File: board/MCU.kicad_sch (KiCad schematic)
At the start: 23 parts, among them SW1 SW_Push, U1 STSPIN32G4TR

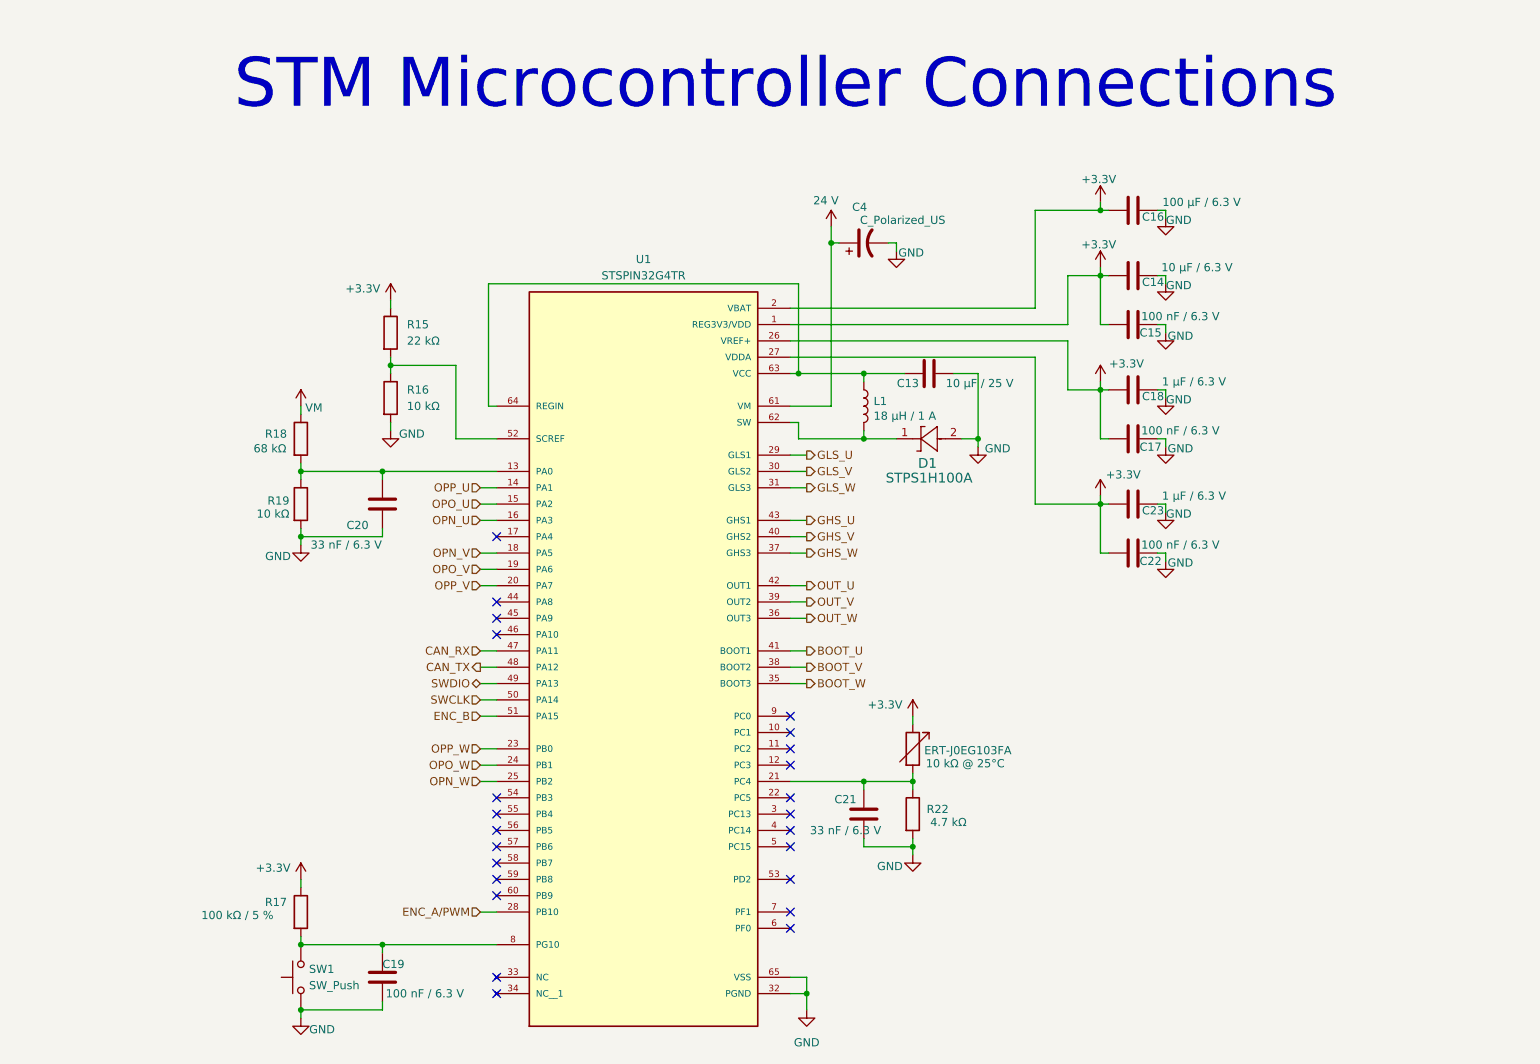
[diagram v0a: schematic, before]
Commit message: Fixed everything mentioned in schematic review, should be ready for second review/layout.
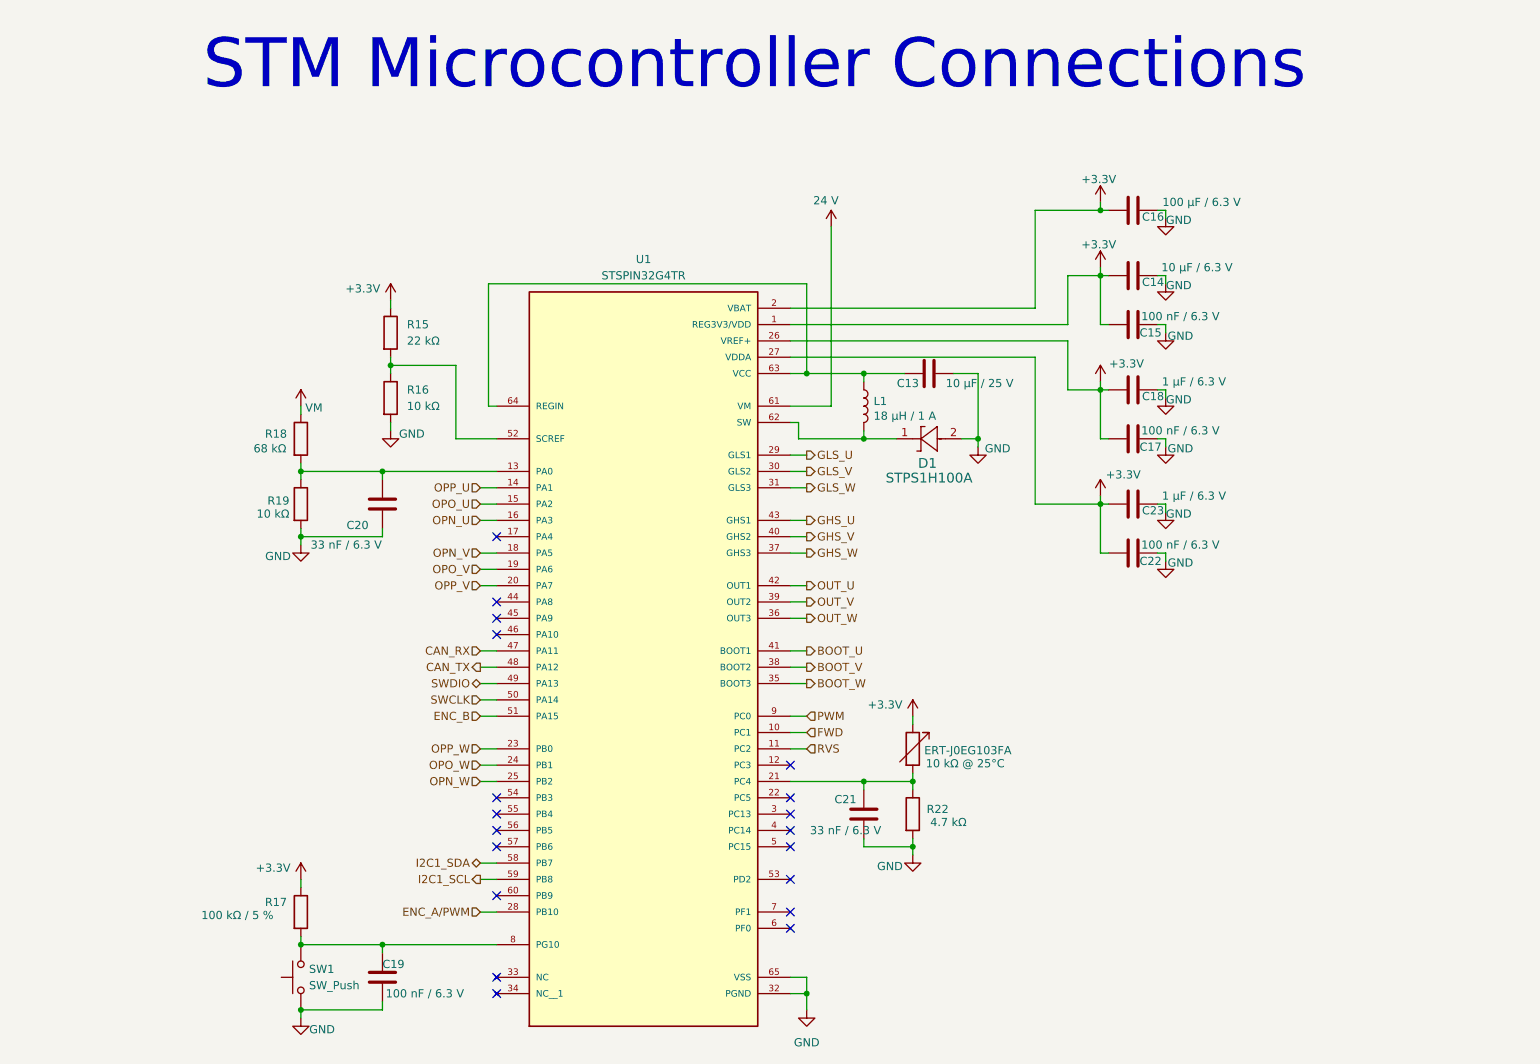
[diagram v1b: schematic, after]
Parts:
- removed C4: C_Polarized_US, symbol Device:C_Polarized_US
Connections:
- net FWD: now reaches U1.10 (PC1)
- net RVS: now reaches U1.11 (PC2)
- net I2C1_SDA: now reaches U1.58 (PB7)
- net I2C1_SCL: now reaches U1.59 (PB8)
- net PWM: now reaches U1.9 (PC0)
- no-connect marks 24 -> 19
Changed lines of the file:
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@@
 	(text "STM Microcontroller Connections\n"
 		(exclude_from_sim no)
-		(at 144.018 28.702 0)
+		(at 139.192 25.654 0)
 		(effects
 			(font
@@
 	)
 	(junction
-		(at 146.05 73.66)
+		(at 147.32 73.66)
 		(diameter 0)
 		(color 0 0 0 0)
@@
 	)
 	(junction
-		(at 151.13 53.34)
-		(diameter 0)
-		(color 0 0 0 0)
-	)
-	(junction
 		(at 156.21 83.82)
 		(diameter 0)
@@
 	)
 	(no_connect
-		(at 144.78 127)
-	)
-	(no_connect
 		(at 99.06 167.64)
 	)
@@
 	)
 	(no_connect
-		(at 144.78 132.08)
-	)
-	(no_connect
 		(at 144.78 147.32)
 	)
@@
 	)
 	(no_connect
-		(at 99.06 152.4)
-	)
-	(no_connect
-		(at 144.78 129.54)
-	)
-	(no_connect
 		(at 99.06 139.7)
 	)
@@
 	)
 	(no_connect
-		(at 99.06 149.86)
-	)
-	(no_connect
 		(at 144.78 157.48)
 	)
@@
 	(wire
 		(pts
-			(xy 151.13 53.34) (xy 152.4 53.34)
+			(xy 96.52 101.6) (xy 99.06 101.6)
 		)
 		(stroke
@@
 	(wire
 		(pts
-			(xy 96.52 101.6) (xy 99.06 101.6)
+			(xy 144.78 119.38) (xy 147.32 119.38)
 		)
 		(stroke
@@
 	(wire
 		(pts
-			(xy 144.78 119.38) (xy 147.32 119.38)
+			(xy 68.58 78.74) (xy 68.58 80.01)
 		)
 		(stroke
@@
 	(wire
 		(pts
-			(xy 68.58 78.74) (xy 68.58 80.01)
+			(xy 194.31 48.26) (xy 193.04 48.26)
 		)
 		(stroke
@@
 	(wire
 		(pts
-			(xy 194.31 48.26) (xy 193.04 48.26)
+			(xy 97.79 78.74) (xy 99.06 78.74)
 		)
 		(stroke
@@
 	(wire
 		(pts
-			(xy 97.79 78.74) (xy 99.06 78.74)
+			(xy 147.32 59.69) (xy 147.32 73.66)
 		)
 		(stroke
@@
 	(wire
 		(pts
-			(xy 146.05 59.69) (xy 146.05 73.66)
+			(xy 151.13 50.8) (xy 151.13 78.74)
 		)
 		(stroke
@@
 	(wire
 		(pts
-			(xy 146.05 73.66) (xy 144.78 73.66)
+			(xy 144.78 73.66) (xy 147.32 73.66)
 		)
 		(stroke
@@
 	(wire
 		(pts
+			(xy 144.78 129.54) (xy 147.32 129.54)
+		)
+		(stroke
+			(width 0)
+			(type default)
+		)
+	)
+	(wire
+		(pts
 			(xy 193.04 58.42) (xy 193.04 66.04)
 		)
@@
 	(wire
 		(pts
-			(xy 151.13 53.34) (xy 151.13 78.74)
-		)
-		(stroke
-			(width 0)
-			(type default)
-		)
-	)
-	(wire
-		(pts
 			(xy 96.52 137.16) (xy 99.06 137.16)
 		)
@@
 	(wire
 		(pts
-			(xy 161.29 53.34) (xy 160.02 53.34)
+			(xy 144.78 91.44) (xy 147.32 91.44)
 		)
 		(stroke
@@
 	(wire
 		(pts
-			(xy 144.78 91.44) (xy 147.32 91.44)
+			(xy 193.04 74.93) (xy 193.04 76.2)
 		)
 		(stroke
@@
 	(wire
 		(pts
-			(xy 193.04 74.93) (xy 193.04 76.2)
+			(xy 96.52 119.38) (xy 99.06 119.38)
 		)
 		(stroke
@@
 	(wire
 		(pts
-			(xy 96.52 119.38) (xy 99.06 119.38)
+			(xy 163.83 137.16) (xy 156.21 137.16)
 		)
 		(stroke
@@
 	(wire
 		(pts
-			(xy 163.83 137.16) (xy 156.21 137.16)
+			(xy 81.28 88.9) (xy 68.58 88.9)
 		)
 		(stroke
@@
 	(wire
 		(pts
-			(xy 81.28 88.9) (xy 68.58 88.9)
+			(xy 81.28 88.9) (xy 81.28 90.17)
 		)
 		(stroke
@@
 	(wire
 		(pts
-			(xy 81.28 88.9) (xy 81.28 90.17)
+			(xy 96.52 152.4) (xy 99.06 152.4)
 		)
 		(stroke
@@
 	(wire
 		(pts
-			(xy 161.29 54.61) (xy 161.29 53.34)
+			(xy 147.32 73.66) (xy 156.21 73.66)
 		)
 		(stroke
@@
 	(wire
 		(pts
-			(xy 151.13 50.8) (xy 151.13 53.34)
-		)
-		(stroke
-			(width 0)
-			(type default)
-		)
-	)
-	(wire
-		(pts
 			(xy 92.71 83.82) (xy 99.06 83.82)
 		)
@@
 	(wire
 		(pts
+			(xy 144.78 132.08) (xy 147.32 132.08)
+		)
+		(stroke
+			(width 0)
+			(type default)
+		)
+	)
+	(wire
+		(pts
 			(xy 96.52 127) (xy 99.06 127)
 		)
@@
 	(wire
 		(pts
+			(xy 144.78 127) (xy 147.32 127)
+		)
+		(stroke
+			(width 0)
+			(type default)
+		)
+	)
+	(wire
+		(pts
 			(xy 203.2 48.26) (xy 201.93 48.26)
 		)
@@
 	(wire
 		(pts
-			(xy 97.79 59.69) (xy 146.05 59.69)
+			(xy 97.79 59.69) (xy 147.32 59.69)
 		)
 		(stroke
@@
 	(wire
 		(pts
-			(xy 146.05 73.66) (xy 156.21 73.66)
+			(xy 144.78 78.74) (xy 151.13 78.74)
 		)
 		(stroke
@@
 	(wire
 		(pts
-			(xy 144.78 78.74) (xy 151.13 78.74)
+			(xy 96.52 149.86) (xy 99.06 149.86)
 		)
 		(stroke
@@
 		)
 	)
+	(hierarchical_label "I2C1_SDA"
+		(shape bidirectional)
+		(at 96.52 149.86 180)
+		(effects
+			(font
+				(size 1.27 1.27)
+			)
+			(justify right)
+		)
+	)
 	(hierarchical_label "BOOT_U"
 		(shape output)
@@
 		)
 	)
+	(hierarchical_label "PWM"
+		(shape input)
+		(at 147.32 127 0)
+		(effects
+			(font
+				(size 1.27 1.27)
+			)
+			(justify left)
+		)
+	)
 	(hierarchical_label "GLS_W"
 		(shape output)
@@
 		)
 	)
+	(hierarchical_label "FWD"
+		(shape input)
+		(at 147.32 129.54 0)
+		(effects
+			(font
+				(size 1.27 1.27)
+			)
+			(justify left)
+		)
+	)
 	(hierarchical_label "BOOT_W"
 		(shape output)
@@
 		)
 	)
+	(hierarchical_label "RVS"
+		(shape input)
+		(at 147.32 132.08 0)
+		(effects
+			(font
+				(size 1.27 1.27)
+			)
+			(justify left)
+		)
+	)
 	(hierarchical_label "OUT_V"
 		(shape output)
@@
 		)
 	)
+	(hierarchical_label "I2C1_SCL"
+		(shape output)
+		(at 96.52 152.4 180)
+		(effects
+			(font
+				(size 1.27 1.27)
+			)
+			(justify right)
+		)
+	)
 	(hierarchical_label "OPO_W"
 		(shape input)
@@
 	)
 	(symbol
-		(lib_id "power:GND")
-		(at 161.29 54.61 0)
-		(unit 1)
-		(exclude_from_sim no)
-		(in_bom yes)
-		(on_board yes)
-		(dnp no)
-		(property "Reference" "#PWR013"
-			(at 161.29 60.96 0)
-			(effects
-				(font
-					(size 1.27 1.27)
-				)
-				(hide yes)
-			)
-		)
-		(property "Value" "GND"
-			(at 163.576 54.864 0)
-			(effects
-				(font
-					(size 1.27 1.27)
-				)
-			)
-		)
-		(property "Footprint" ""
-			(at 161.29 54.61 0)
-			(effects
-				(font
-					(size 1.27 1.27)
-				)
-				(hide yes)
-			)
-		)
-		(property "Datasheet" ""
-			(at 161.29 54.61 0)
-			(effects
-				(font
-					(size 1.27 1.27)
-				)
-				(hide yes)
-			)
-		)
-		(property "Description" "Power symbol creates a global label with name \"GND\" , ground"
-			(at 161.29 54.61 0)
-			(effects
-				(font
-					(size 1.27 1.27)
-				)
-				(hide yes)
-			)
-		)
-		(pin "1"
-		)
-		(instances
-			(project ""
-				(path "/1ef8bc88-f0df-4a97-862b-c4b9ec3b4ed0/02edeb2f-867a-4e66-ac0c-df2434256428"
-					(reference "#PWR013")
-					(unit 1)
-				)
-			)
-		)
-	)
-	(symbol
 		(lib_id "power:+3.3V")
 		(at 193.04 46.99 0)
@@
 					(unit 1)
 				)
-			)
-		)
-	)
-	(symbol
-		(lib_id "Device:C_Polarized_US")
-		(at 156.21 53.34 90)
-		(unit 1)
-		(exclude_from_sim no)
-		(in_bom yes)
-		(on_board yes)
-		(dnp no)
-		(property "Reference" "C4"
-			(at 156.718 47.752 90)
-			(effects
-				(font
-					(size 1.27 1.27)
-				)
-				(justify left)
-			)
-		)
-		(property "Value" "C_Polarized_US"
-			(at 168.91 49.784 90)
-			(effects
-				(font
-					(size 1.27 1.27)
-				)
-				(justify left)
-			)
-		)
-		(property "Footprint" ""
-			(at 156.21 53.34 0)
-			(effects
-				(font
-					(size 1.27 1.27)
-				)
-				(hide yes)
-			)
-		)
-		(property "Datasheet" "~"
-			(at 156.21 53.34 0)
-			(effects
-				(font
-					(size 1.27 1.27)
-				)
-				(hide yes)
-			)
-		)
-		(property "Description" "Polarized capacitor, US symbol"
-			(at 156.21 53.34 0)
-			(effects
-				(font
-					(size 1.27 1.27)
-				)
-				(hide yes)
-			)
-		)
-		(pin "1"
-		)
-		(pin "2"
-		)
-		(instances
-			(project ""
-				(path "/1ef8bc88-f0df-4a97-862b-c4b9ec3b4ed0/02edeb2f-867a-4e66-ac0c-df2434256428"
-					(reference "C4")
-					(unit 1)
-				)

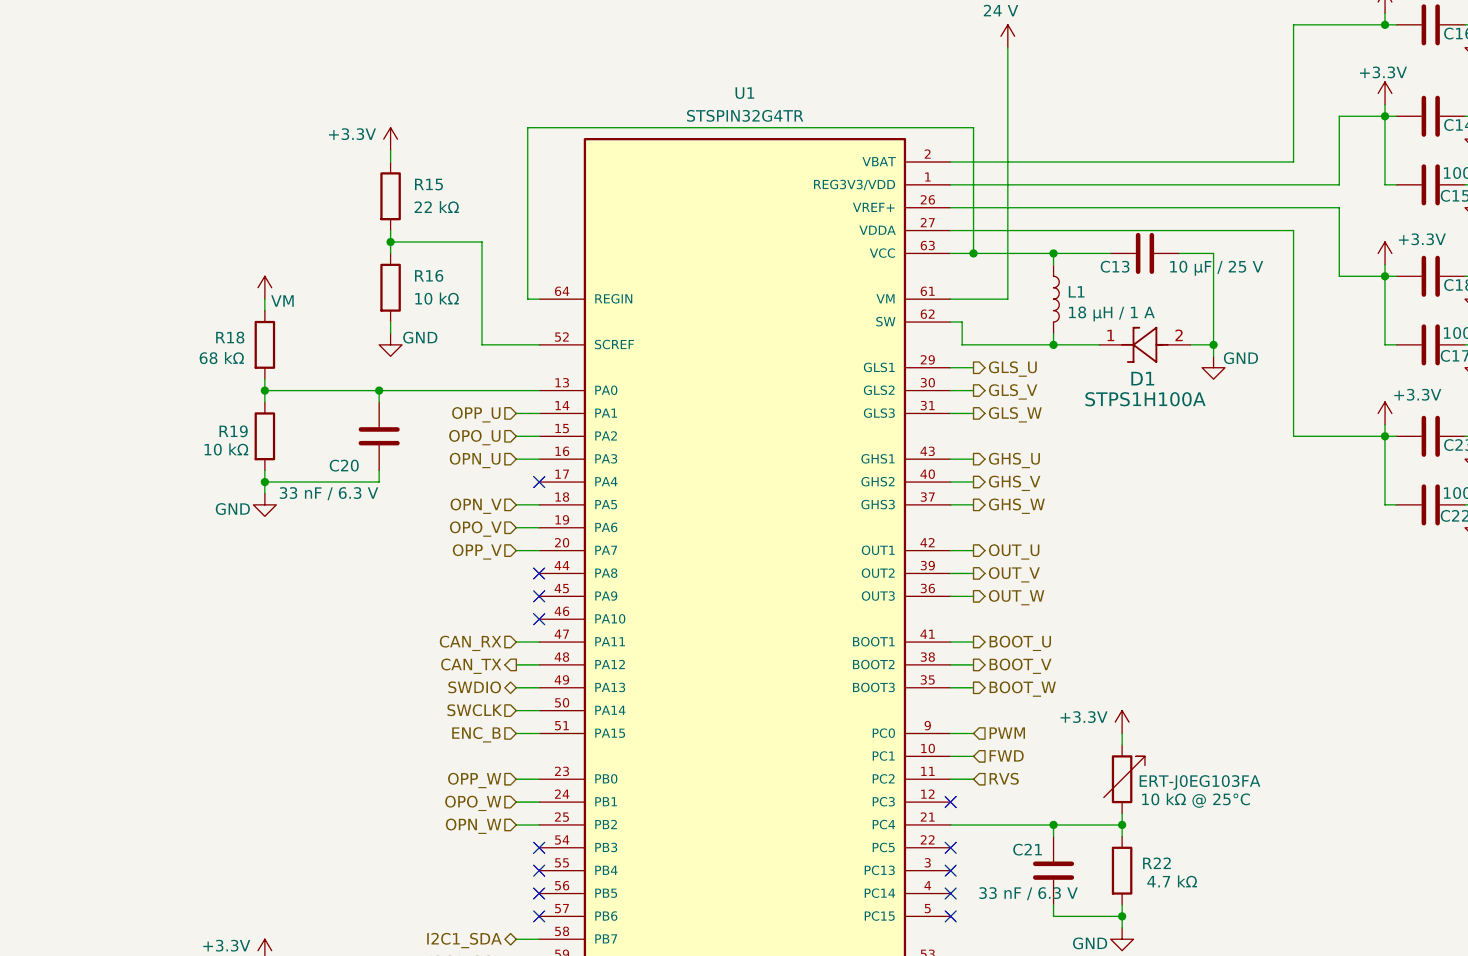
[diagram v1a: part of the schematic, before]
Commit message: Updated footprints for schematic
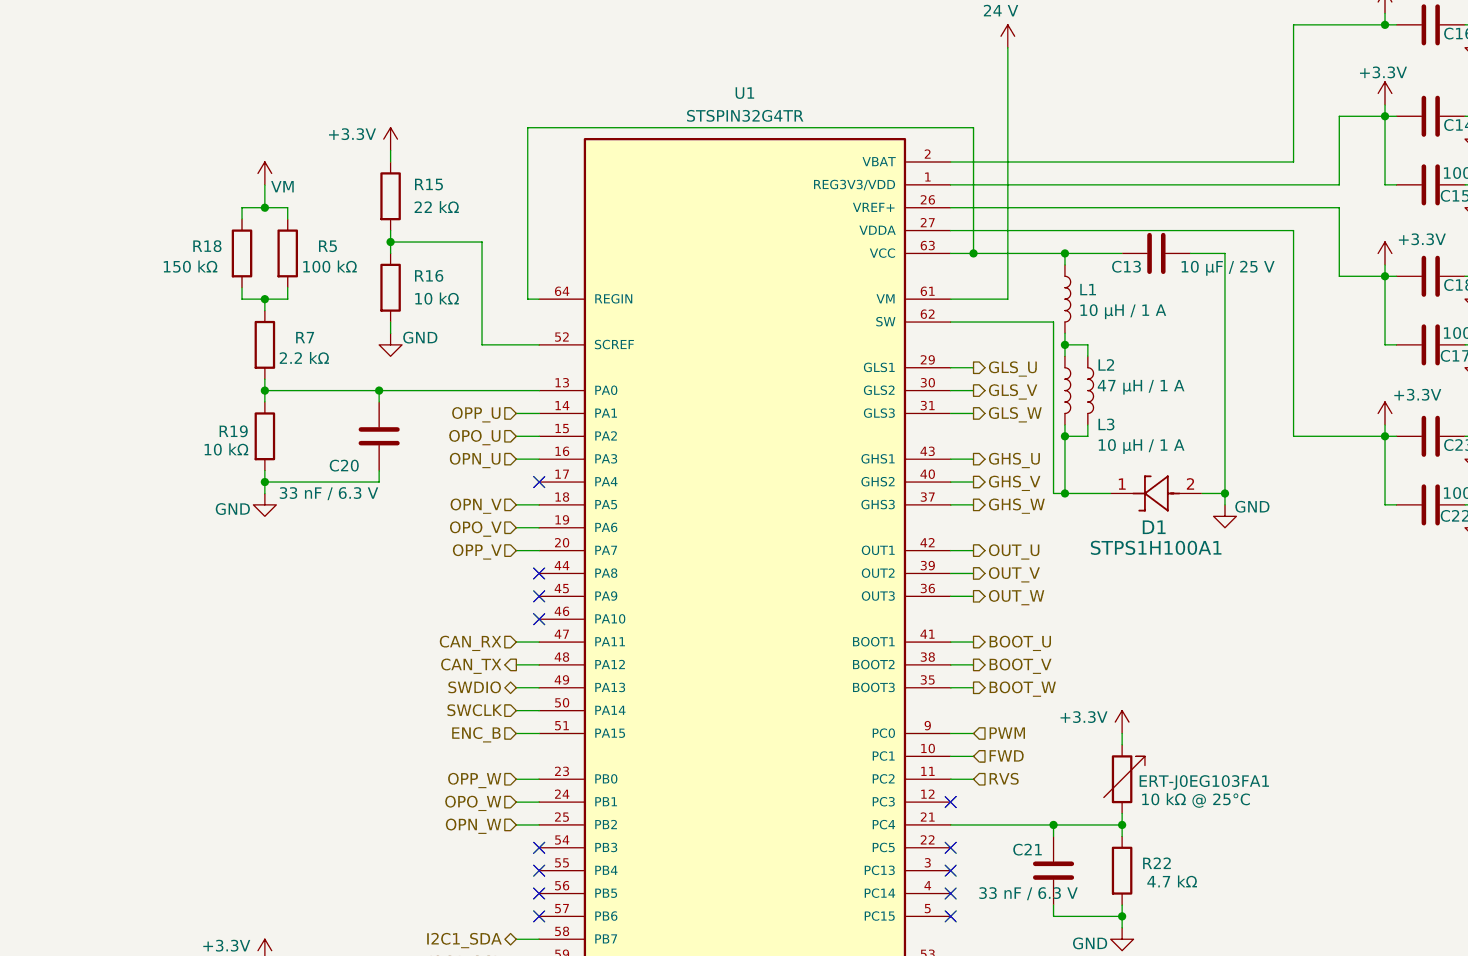
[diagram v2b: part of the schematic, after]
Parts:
- added L2: 47 μH / 1 A, BrushlessMocoBoard:IND_VLS5045EX-470M, symbol Device:L
- added L3: 10 μH / 1 A, Inductor_SMD:L_1008_2520Metric_Pad1.43x2.20mm_HandSolder, symbol Device:L
- added R5: 100 kΩ, Resistor_SMD:R_0603_1608Metric_Pad0.98x0.95mm_HandSolder, symbol Device:R
- added R7: 2.2 kΩ, Resistor_SMD:R_0603_1608Metric_Pad0.98x0.95mm_HandSolder, symbol Device:R
- C13: footprint (none) -> BrushlessMocoBoard:CAPPRD250W45D400H700
- C14, C15, C17, C19, C22: footprint (none) -> Capacitor_SMD:C_0603_1608Metric_Pad1.08x0.95mm_HandSolder
- C16: footprint (none) -> Capacitor_SMD:C_1206_3216Metric_Pad1.33x1.80mm_HandSolder
- C18, C23: footprint (none) -> Capacitor_SMD:C_0402_1005Metric_Pad0.74x0.62mm_HandSolder
- C20, C21: footprint (none) -> Capacitor_SMD:C_0201_0603Metric_Pad0.64x0.40mm_HandSolder
- ERT-J0EG103FA1: renamed from ERT-J0EG103FA; footprint (none) -> Resistor_SMD:R_0402_1005Metric_Pad0.72x0.64mm_HandSolder
- L1: value 18 μH / 1 A -> 10 μH / 1 A; footprint (none) -> Inductor_SMD:L_1008_2520Metric_Pad1.43x2.20mm_HandSolder
- R15, R16, R17, R19, R22: footprint (none) -> Resistor_SMD:R_0603_1608Metric_Pad0.98x0.95mm_HandSolder
- R18: value 68 kΩ -> 150 kΩ; footprint (none) -> Resistor_SMD:R_0603_1608Metric_Pad0.98x0.95mm_HandSolder
- STPS1H100A1: renamed from STPS1H100A; footprint SMA_STM -> BoCoFootprintLibrary:SMA_STM
- SW1: footprint (none) -> MRDT_Switches:SW_SPST_TL3305A
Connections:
- net VM: now also R5.1
- net at C20.1, R19.1, U1.13 (PA0): now also R7.2; no longer R18.2
- net at STPS1H100A1.1, U1.62 (SW): now also L2.2, L3.2; no longer L1.2
- new net: L1.2, L2.1, L3.1
- new net: R18.2, R5.2, R7.1
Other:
- moved on the sheet: C13, L1, R18, STPS1H100A1
